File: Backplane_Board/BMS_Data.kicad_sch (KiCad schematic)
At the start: 8 parts, among them J4 Conn_01x07_Female, U2 PINA740AIREMR

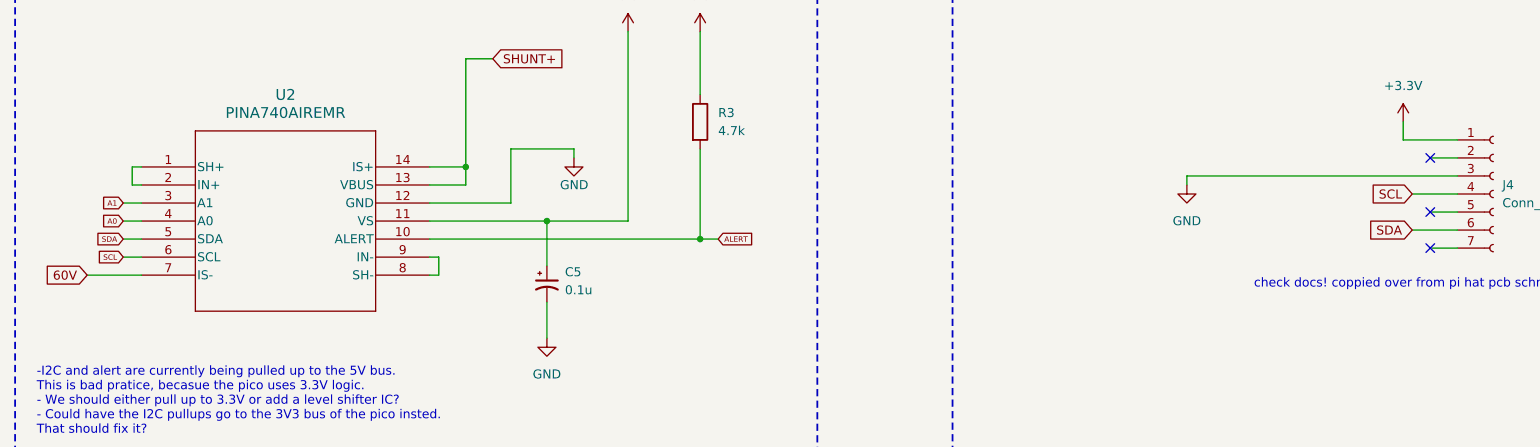
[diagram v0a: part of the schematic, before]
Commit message: rough layout compleat, 200+ drc errors to fix
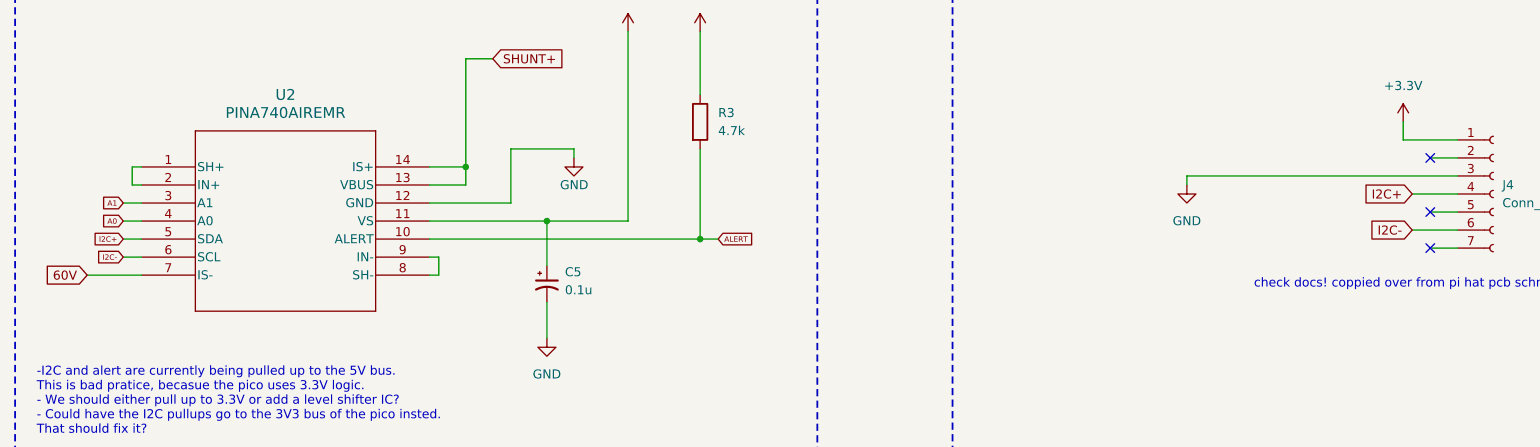
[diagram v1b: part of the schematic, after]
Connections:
- net SCL: no longer J4.4 (Pin_4), U2.6 (SCL)
- net SDA renamed I2C+
- net I2C+: now also J4.4 (Pin_4); no longer J4.6 (Pin_6)
- new net I2C-: J4.6 (Pin_6), U2.6 (SCL)
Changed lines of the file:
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@@
 		)
 	)
-	(global_label "SCL"
+	(global_label "I2C-"
 		(shape input)
 		(at 36.83 135.89 180)
@@
 		)
 		(property "Intersheetrefs" "${INTERSHEET_REFS}"
-			(at 32.934 135.89 0)
+			(at 32.2446 135.89 0)
 			(effects
 				(font
@@
 		)
 	)
-	(global_label "SDA"
+	(global_label "I2C-"
 		(shape input)
 		(at 218.44 132.08 180)
@@
 		)
 		(property "Intersheetrefs" "${INTERSHEET_REFS}"
-			(at 211.8867 132.08 0)
+			(at 210.7981 132.08 0)
 			(effects
 				(font
@@
 		)
 	)
-	(global_label "SCL"
+	(global_label "I2C+"
 		(shape input)
 		(at 218.44 127 180)
@@
 		)
 		(property "Intersheetrefs" "${INTERSHEET_REFS}"
-			(at 211.9472 127 0)
+			(at 210.7981 127 0)
 			(effects
 				(font
@@
 		)
 	)
-	(global_label "SDA"
+	(global_label "I2C+"
 		(shape input)
 		(at 36.83 133.35 180)
@@
 		)
 		(property "Intersheetrefs" "${INTERSHEET_REFS}"
-			(at 32.8978 133.35 0)
+			(at 32.2446 133.35 0)
 			(effects
 				(font

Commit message: few drc errors left - must fix fet footprints
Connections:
- net SCL is gone; now on net I2C-: JP1.2 (B), JP2.2 (B)
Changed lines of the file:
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@@
 		)
 	)
-	(global_label "SCL"
+	(global_label "I2C-"
 		(shape input)
 		(at 252.73 40.64 0)
@@
 		)
 		(property "Intersheetrefs" "${INTERSHEET_REFS}"
-			(at 259.2228 40.64 0)
+			(at 260.3719 40.64 0)
 			(effects
 				(font
@@
 		)
 	)
-	(global_label "SCL"
+	(global_label "I2C-"
 		(shape input)
 		(at 205.74 40.64 0)
@@
 		)
 		(property "Intersheetrefs" "${INTERSHEET_REFS}"
-			(at 212.2328 40.64 0)
-			(effects
-				(font
+			(at 213.3819 40.64 0)
+			(effects
+				(font

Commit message: clean up
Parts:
- added H1, H2, H3, H4: MountingHole_Pad, MountingHole:MountingHole_4.3mm_M4_Pad_Via, symbol Mechanical:MountingHole_Pad
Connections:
- net GND: now also H1.1, H2.1, H3.1, H4.1
